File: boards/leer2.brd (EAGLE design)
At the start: 30 x 56 mm, 61 parts, among them IC1 XMEGA128A1, IC2 7805DT, Q1 BC846BSMD, Q2 BC846BSMD, Q3 BC846BSMD, Q4 BC846BSMD, Q5 BC846BSMD, Q6 BC846BSMD, Q7 BC846BSMD, Q8 BC846BSMD

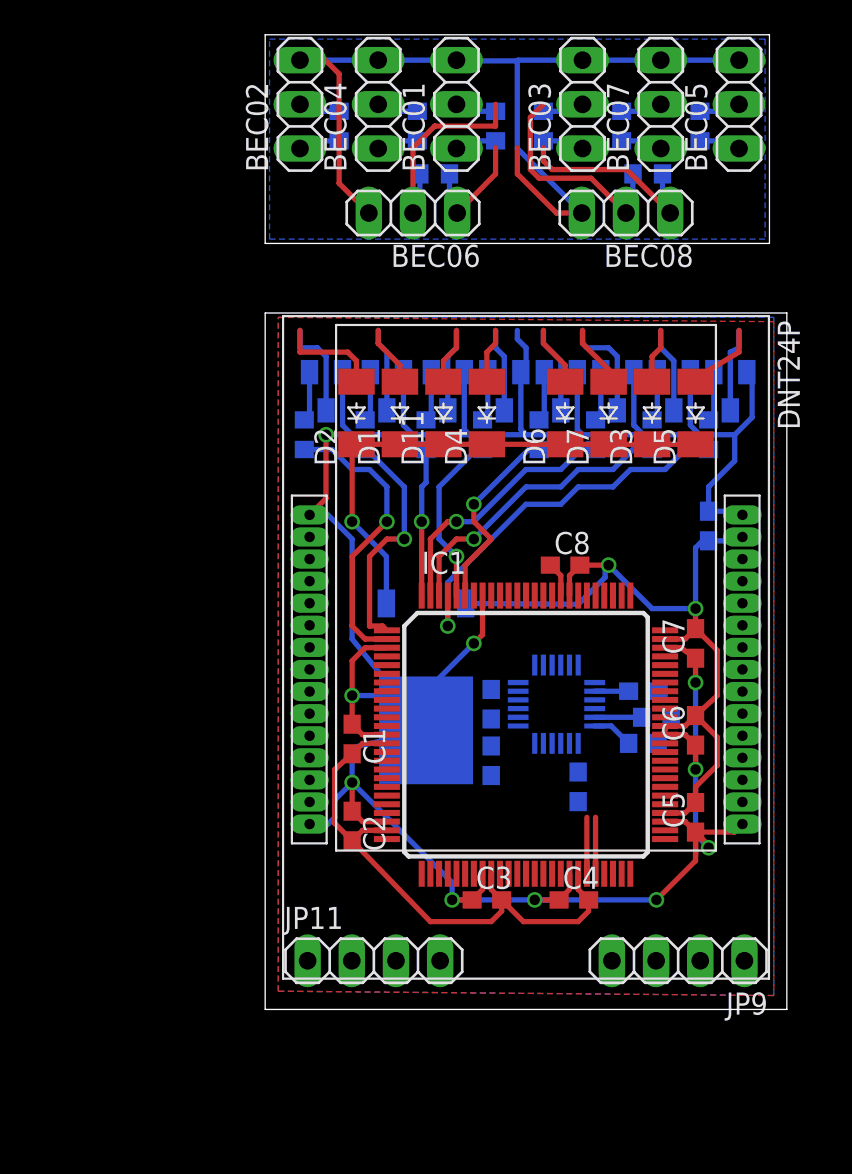
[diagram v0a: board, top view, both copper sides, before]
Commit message: - more board changes - we-direkt design rule check modifications - made editable with eagle lite again
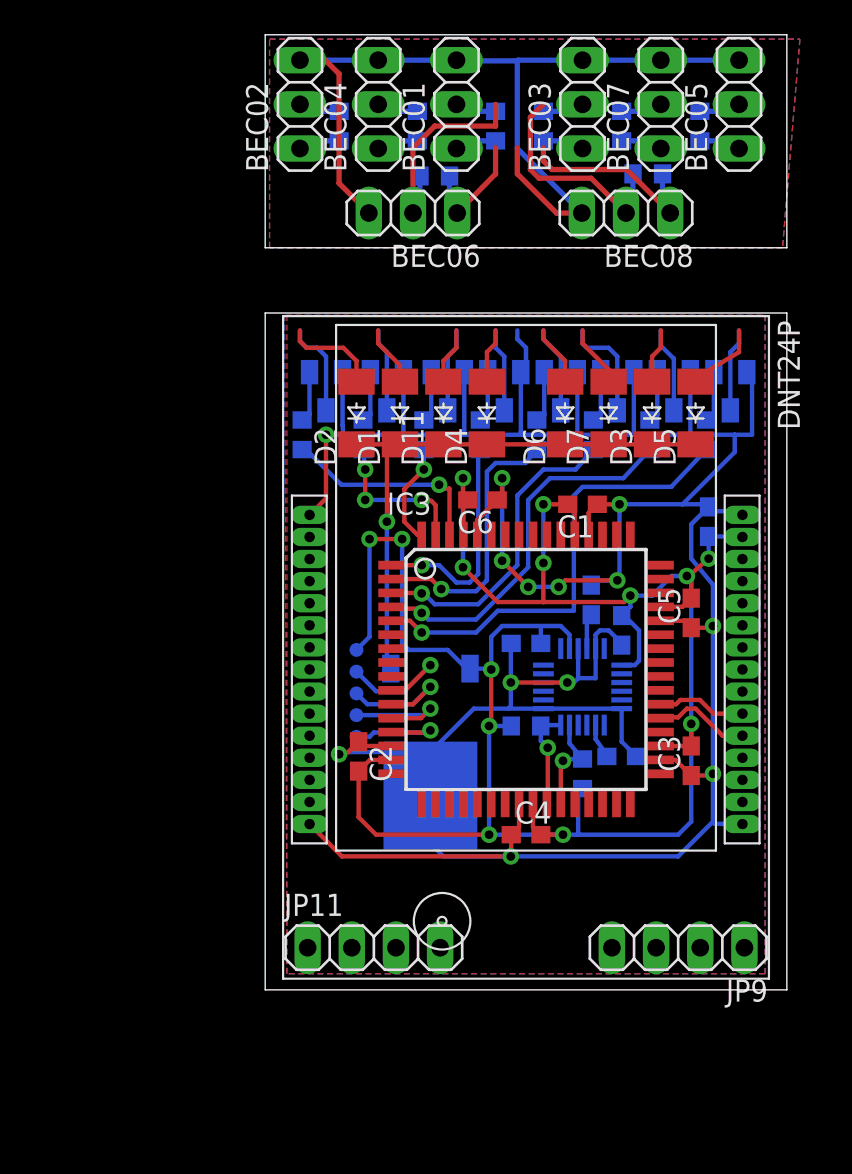
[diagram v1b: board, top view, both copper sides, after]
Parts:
- removed C7, C8: (no value), eagle-ltspice:C0603
- removed IC1: XMEGA128A1, atmel:TQFP100
- added IC3: (no value), ATxmega__A3:TQFP-64
- added TP1, TP2, TP3, TP4, TP7: TPTP08R, testpad:TP08R
- moved C1 18.9 mm to (19.2, 29.0), turned to 180 degrees
- moved C6 18.0 mm to (13.5, 29.2), turned to 180 degrees
- moved C3 14.2 mm to (25.5, 14.2), turned to 90 degrees
- moved C5 11.8 mm to (25.5, 22.8)
- moved C14 9.34 mm to (21.5, 21.8), turned to 90 degrees
- moved C13 8.31 mm to (19.8, 23.5), turned to 270 degrees
- moved C12 7.04 mm to (16.0, 21.0), turned to 180 degrees
- moved R20 6.82 mm to (16.0, 16.2), turned to 180 degrees
- moved R17 5.35 mm to (19.2, 13.5), turned to 90 degrees
- moved C4 4.65 mm to (16.0, 10.0)
- moved C2 4.02 mm to (6.38, 14.5)
- moved C10 3.95 mm to (21.5, 14.5)
- moved IC2 3.76 mm to (10.5, 14.8)
- moved U$3 1.80 mm to (19.2, 18.5), turned to 180 degrees
- moved JP11 0.75 mm to (7.25, 3.50)
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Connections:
- removed net AVCC: IC1.4
- removed net AVCC1: IC1.94
- new net N$38: IC3.10, TP3.TP
- new net N$39: IC3.11, TP2.TP
- new net N$40: IC3.12, TP1.TP
- new net N$41: IC3.13, TP7.TP
- net +3V3: now also IC3.15, IC3.25, IC3.35, IC3.45, IC3.53, IC3.61, TP4.TP; no longer C7.2, C8.2, IC1.14, IC1.24, IC1.34, IC1.44, IC1.54, IC1.64, IC1.74, IC1.83
- net GND: now also IC3.14, IC3.24, IC3.34, IC3.44, IC3.52, IC3.60; no longer C7.1, C8.1, IC1.13, IC1.23, IC1.3, IC1.33, IC1.43, IC1.53, IC1.63, IC1.73, IC1.84, IC1.93
- net N$25: now also IC3.63; no longer IC1.1
- net N$26: now also IC3.64; no longer IC1.100
- net N$27: now also IC3.5; no longer IC1.97
- net N$28: now also IC3.4, R13.1; no longer IC1.96, R11.1
- net N$29: now also IC3.62; no longer IC1.2
- net N$30: now also IC3.1, R11.1; no longer IC1.98, R13.1
- net N$31: now also IC3.2, R15.1; no longer IC1.99, R7.1
- net N$32: now also IC3.3, R7.1; no longer IC1.95, R15.1
- net N$33: now also IC3.37; no longer IC1.88
- net N$36: now also IC3.38; no longer IC1.87
- net PF0: now also IC3.26; no longer IC1.46
- net PF1: now also IC3.27; no longer IC1.45
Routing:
- net +3V3: track 78.5 -> 133.7 mm, vias 2 -> 14
- net GND: track 233.0 -> 260.2 mm, vias 10 -> 13
- net N$28: track 10.1 -> 21.5 mm
- net N$38: track 0.00 -> 8.19 mm, vias 0 -> 1
- net N$39: track 0.00 -> 7.59 mm, vias 0 -> 1
- net N$40: track 0.00 -> 6.88 mm, vias 0 -> 1
- net N$41: track 0.00 -> 6.72 mm, vias 0 -> 1
- net N$32: track 11.3 -> 18.0 mm
- net N$33: track 0.00 -> 5.57 mm
- net N$36: track 0.00 -> 5.13 mm
- net N$25: track 13.7 -> 8.76 mm, vias 1 -> 3
- net N$29: track 16.8 -> 12.3 mm
- net N$27: track 22.4 -> 26.7 mm
- net N$30: track 17.0 -> 12.8 mm
- net N$34: track 29.7 -> 32.7 mm
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- added copper zone on layer 16, net POLY1
- added copper zone on layer 1, net POLY2
- added copper zone on layer 1, net POLY3
- added copper zone on layer 16, net POLY4
- removed copper zone on layer 1, net GNDS
- removed copper zone on layer 16, net GNDS
- removed copper zone on layer 16, net S$1
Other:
- board size 30 x 56 mm -> 30 x 54.9 mm

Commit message: Board passes drc checks for we-direkt and itead now
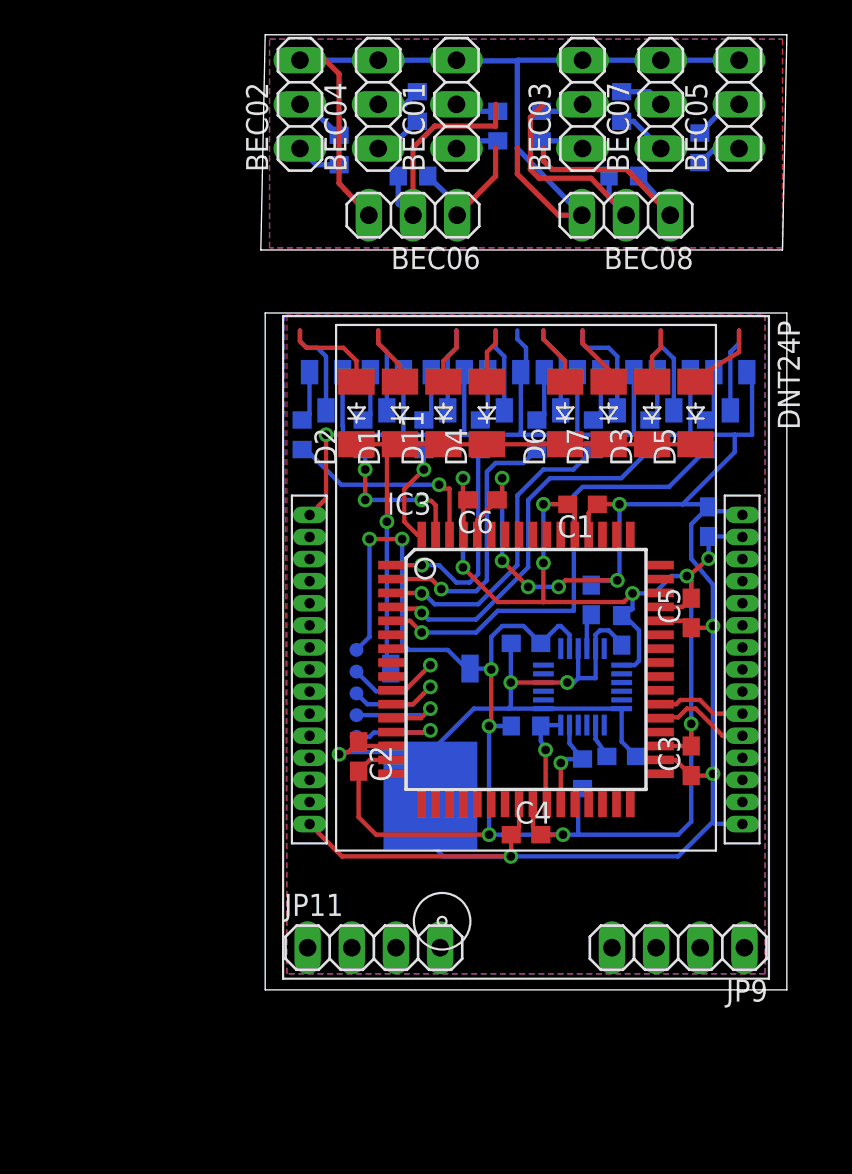
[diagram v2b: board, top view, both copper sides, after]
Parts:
- moved R16 1.38 mm to (21.6, 47.9)
- moved R6 1.38 mm to (5.25, 49.4)
- moved R10 1.25 mm to (26.0, 49.5)
- moved R12 1.25 mm to (9.50, 47.9)
- moved R14 1.12 mm to (21.5, 51.9)
- moved R2 1.12 mm to (9.75, 51.9)
- moved BEC06 0.12 mm to (9.50, 45.6)
- moved BEC08 0.12 mm to (21.8, 45.6)
- moved R4 0.12 mm to (14.4, 50.8)
- moved R8 0.12 mm to (16.9, 50.8)
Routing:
- net N$16: track 11.8 -> 12.6 mm
- net N$22: track 16.7 -> 17.3 mm
- net N$6: track 7.96 -> 8.49 mm
- net N$12: track 6.78 -> 7.30 mm
- net N$17: track 15.7 -> 16.2 mm
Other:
- board size 30 x 54.9 mm -> 30.2 x 54.9 mm

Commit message: Updated Board with Voltage-Sensing Circuit
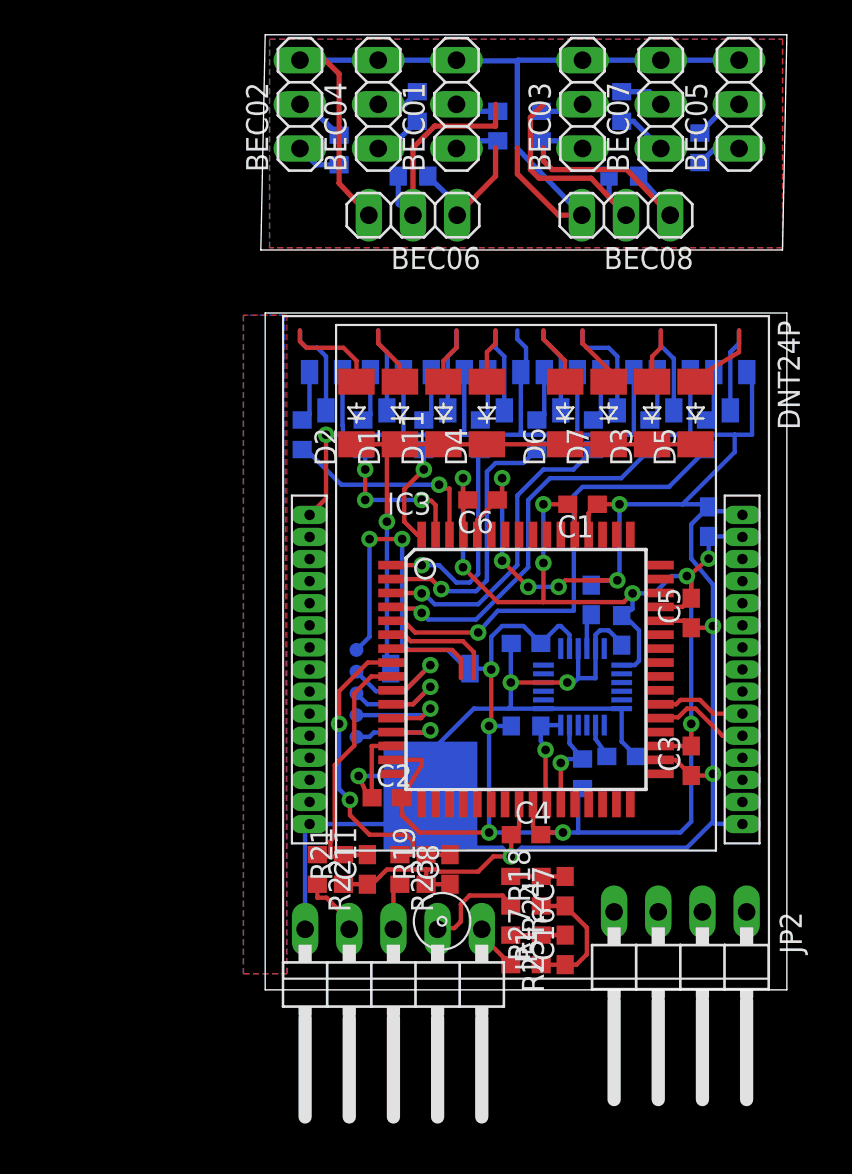
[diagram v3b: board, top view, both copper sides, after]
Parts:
- removed JP11, JP9: (no value), pinhead:1X04
- added C11, C16, C7, C8: (no value), eagle-ltspice:C0603
- added JP1: (no value), pinhead:1X05/90
- added JP2: (no value), pinhead:1X04/90
- added R18, R19, R21, R22, R23, R24, R25, R27: (no value), eagle-ltspice:R0603
- moved C2 2.88 mm to (8.00, 12.1), turned to 0 degrees
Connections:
- new net N$42: JP1.2, R24.2
- new net N$43: JP1.3, R23.2
- new net N$44: JP1.4, R22.2
- new net N$50: JP1.1, R25.2
- new net PB0: C16.2, IC3.6, R25.1, R27.2
- new net PB1: C7.2, IC3.7, R18.2, R24.1
- new net PB2: C8.2, IC3.8, R19.2, R23.1
- new net PB3: C11.2, IC3.9, R21.2, R22.1
- net GND: now also C11.1, C16.1, C7.1, C8.1, JP1.5, R18.1, R19.1, R21.1, R27.1
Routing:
- net GND: track 260.5 -> 283.6 mm
- net PB2: track 0.00 -> 19.0 mm, vias 0 -> 2
- net PB3: track 0.00 -> 15.4 mm
- net PB0: track 0.00 -> 9.79 mm
- net PB1: track 0.00 -> 8.49 mm
- net N$42: track 0.00 -> 6.55 mm
- net N$44: track 0.00 -> 3.66 mm
- net N$43: track 0.00 -> 2.75 mm
- net N$50: track 0.00 -> 2.73 mm
- net +3V3: track 133.8 -> 131.5 mm

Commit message: Added Barometer
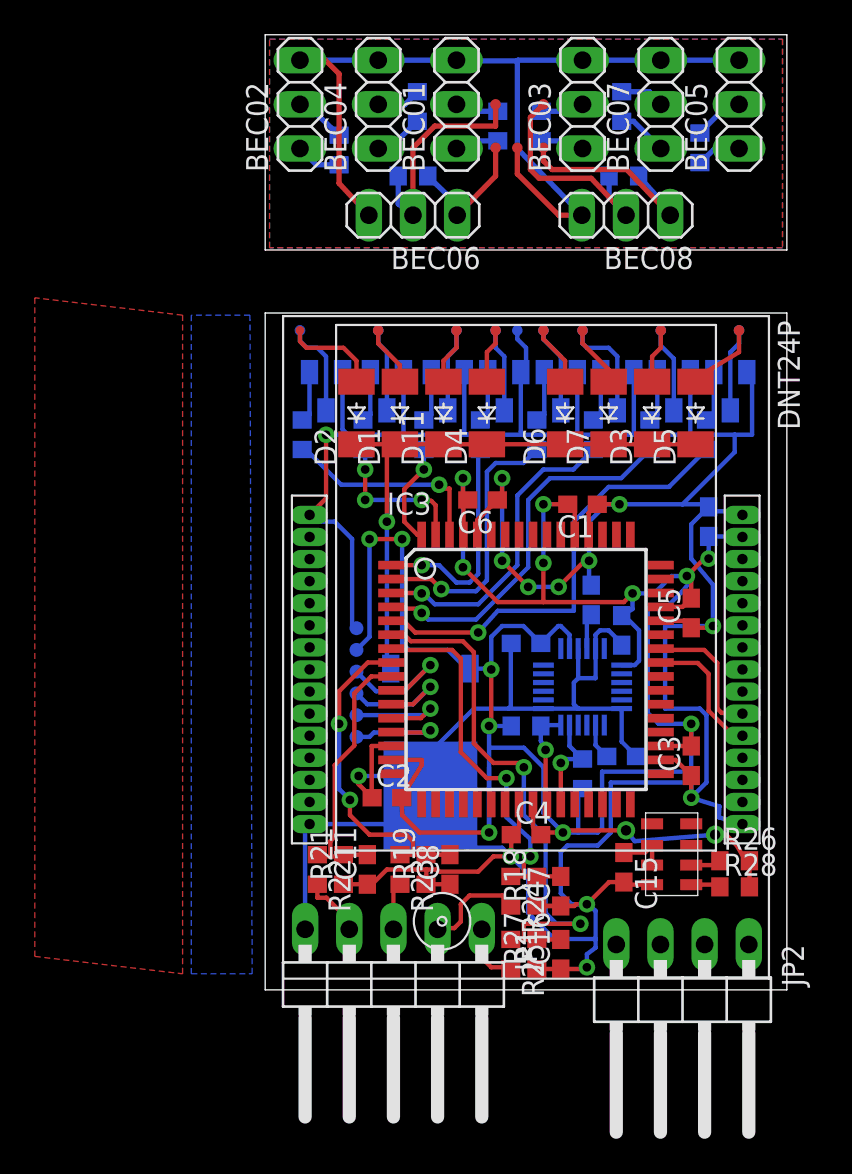
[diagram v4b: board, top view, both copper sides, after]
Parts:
- added C15: (no value), eagle-ltspice:C0603
- added R26, R28: (no value), eagle-ltspice:R0603
- added TP5: TPTP08R, testpad:TP08R
- added U$2: MS5611, ms5611:01BA03
- moved JP2 1.88 mm to (25.0, -0.12)
- moved C16 0.35 mm to (18.0, 3.12)
- moved R27 0.35 mm to (16.6, 3.12)
- moved C7 0.25 mm to (18.0, 6.75)
- moved R18 0.25 mm to (16.6, 6.75)
- moved R25 0.25 mm to (15.1, 3.12)
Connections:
- new net N$46: IC3.40, R28.1, U$2.P$8
- new net N$47: IC3.39, R26.1, U$2.P$7
- net +3V3: now also C15.1, R26.2, R28.2, U$2.P$2, U$2.P$3
- net GND: now also C15.2, TP5.TP, U$2.P$1
- net N$33: now also IC3.41; no longer IC3.37
- net N$36: now also IC3.42; no longer IC3.38
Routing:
- net GND: track 283.6 -> 314.8 mm
- net +3V3: track 131.5 -> 159.0 mm, vias 14 -> 16
- net PB0: track 9.79 -> 32.0 mm, vias 0 -> 2
- net PB1: track 8.49 -> 22.1 mm, vias 0 -> 2
- net N$36: track 5.13 -> 7.77 mm
- net N$33: track 5.57 -> 7.68 mm
- net N$47: track 0.00 -> 1.75 mm
- net N$46: track 0.00 -> 1.70 mm
- net N$27: track 26.7 -> 25.8 mm
- net N$50: track 2.73 -> 3.58 mm
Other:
- board size 30.2 x 54.9 mm -> 30 x 54.9 mm

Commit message: Changed location of barometer
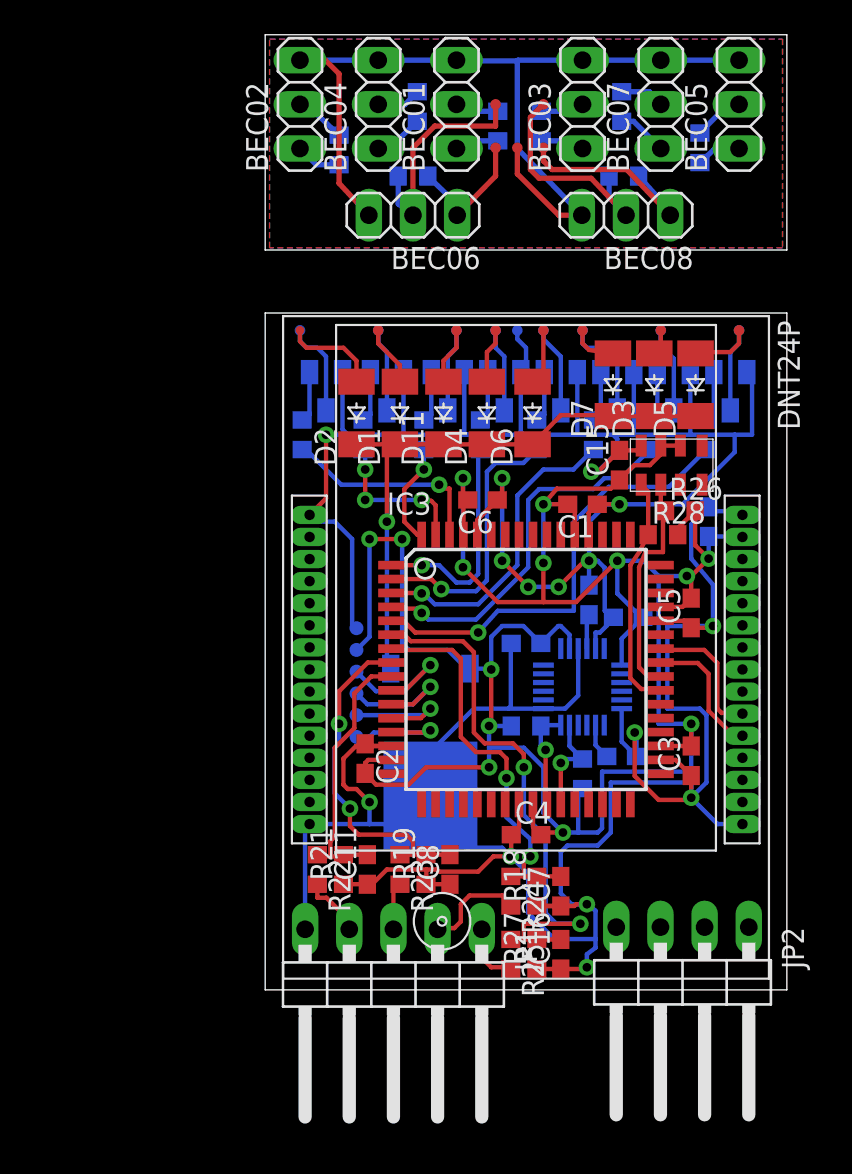
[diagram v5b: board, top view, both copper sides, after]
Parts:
- moved C15 23.1 mm to (21.4, 31.2), turned to 90 degrees
- moved R28 20.7 mm to (23.9, 27.2)
- moved R26 20.4 mm to (24.9, 28.6)
- moved U$2 18.5 mm to (26.8, 29.8), turned to 90 degrees
- moved C2 2.57 mm to (6.75, 14.4), turned to 270 degrees
- moved D6 1.88 mm to (16.4, 34.2)
- moved D7 1.64 mm to (21.0, 35.9)
- moved D3 1.63 mm to (23.4, 35.9)
- moved D5 1.62 mm to (25.8, 35.9)
- moved JP2 1.00 mm to (25.0, 0.88)
- moved C14 0.84 mm to (21.9, 22.5), turned to 180 degrees
- moved C13 0.12 mm to (19.6, 23.5)
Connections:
- net N$46: now also IC3.39; no longer IC3.40
- net N$47: now also IC3.40; no longer IC3.39
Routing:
- net N$47: track 1.75 -> 13.7 mm
- net N$46: track 1.70 -> 13.6 mm
- net +3V3: track 159.0 -> 149.3 mm, vias 16 -> 14
- net GND: track 314.8 -> 323.0 mm, vias 13 -> 15
- net N$20: track 5.73 -> 4.50 mm
- net N$9: track 6.11 -> 5.21 mm
- net N$12: track 7.30 -> 6.41 mm
- net N$34: track 32.7 -> 33.4 mm
- net PB2: track 19.0 -> 19.5 mm
- removed copper zone on layer 1, net POLY3
- removed copper zone on layer 16, net POLY4
